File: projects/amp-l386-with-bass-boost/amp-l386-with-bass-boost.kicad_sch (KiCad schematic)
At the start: 18 parts, among them J1 AudioJack, J2 Jack-DC, U1 LM386

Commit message: Checking initial PCB placement of bassboost project
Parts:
- AudioIn1: renamed from J1; footprint jme-audio-pinheader-2.54-vertical -> jme:jme-audio-pinheader-2.54-vertical
- BassBoost1, Gain1, Volume1: footprint (none) -> Connector_PinHeader_2.54mm:PinHeader_1x03_P2.54mm_Vertical
- U1: footprint LM386:DIP08 -> Package_DIP:DIP-8_W7.62mm_Socket
- renumbered LS1 to AudioOut1, J2 to DC-9V1
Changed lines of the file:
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@@
   )
   (symbol (lib_id "Connector:AudioJack2") (at 77.47 77.47 0) (mirror x) (unit 1)
-    (in_bom yes) (on_board yes) (fields_autoplaced)
-    (property "Reference" "J1" (id 0) (at 72.39 76.8349 0)
+    (in_bom yes) (on_board yes)
+    (property "Reference" "AudioIn1" (id 0) (at 81.28 72.39 0)
       (effects (font (size 1.27 1.27)) (justify right))
     )
     (property "Value" "AudioJack" (id 1) (at 72.39 79.3749 0)
-      (effects (font (size 1.27 1.27)) (justify right))
-    )
-    (property "Footprint" "jme-audio-pinheader-2.54-vertical" (id 2) (at 77.47 77.47 0)
+      (effects (font (size 1.27 1.27)) (justify right) hide)
+    )
+    (property "Footprint" "jme:jme-audio-pinheader-2.54-vertical" (id 2) (at 77.47 77.47 0)
       (effects (font (size 1.27 1.27)) hide)
     )
@@
     (property "Reference" "U1" (id 0) (at 144.78 78.74 0))
     (property "Value" "LM386" (id 1) (at 144.78 81.28 0))
-    (property "Footprint" "LM386:DIP08" (id 2) (at 143.51 82.55 0)
+    (property "Footprint" "Package_DIP:DIP-8_W7.62mm_Socket" (id 2) (at 143.51 82.55 0)
       (effects (font (size 1.27 1.27)) hide)
     )
@@
       (effects (font (size 1.27 1.27)) (justify right))
     )
-    (property "Footprint" "" (id 2) (at 160.02 102.87 0)
+    (property "Footprint" "Connector_PinHeader_2.54mm:PinHeader_1x03_P2.54mm_Vertical" (id 2) (at 160.02 102.87 0)
       (effects (font (size 1.27 1.27)) hide)
     )
@@
   (symbol (lib_id "Device:Speaker") (at 195.58 85.09 0) (unit 1)
     (in_bom yes) (on_board yes) (fields_autoplaced)
-    (property "Reference" "LS1" (id 0) (at 200.66 85.0899 0)
+    (property "Reference" "AudioOut1" (id 0) (at 200.66 85.0899 0)
       (effects (font (size 1.27 1.27)) (justify left))
     )
@@
       (effects (font (size 1.27 1.27)) (justify right))
     )
-    (property "Footprint" "" (id 2) (at 96.52 82.55 0)
+    (property "Footprint" "Connector_PinHeader_2.54mm:PinHeader_1x03_P2.54mm_Vertical" (id 2) (at 96.52 82.55 0)
       (effects (font (size 1.27 1.27)) hide)
     )
@@
   (symbol (lib_id "Connector:Jack-DC") (at 110.49 33.02 0) (unit 1)
     (in_bom yes) (on_board yes)
-    (property "Reference" "J2" (id 0) (at 110.49 21.59 0))
-    (property "Value" "Jack-DC" (id 1) (at 110.49 24.13 0))
+    (property "Reference" "DC-9V1" (id 0) (at 110.49 26.67 0))
+    (property "Value" "Jack-DC" (id 1) (at 110.49 24.13 0)
+      (effects (font (size 1.27 1.27)) hide)
+    )
     (property "Footprint" "Connector_PinHeader_2.54mm:PinHeader_1x02_P2.54mm_Vertical" (id 2) (at 111.76 34.036 0)
       (effects (font (size 1.27 1.27)) hide)
@@
       (effects (font (size 1.27 1.27)) (justify right))
     )
-    (property "Footprint" "" (id 2) (at 157.48 119.38 0)
+    (property "Footprint" "Connector_PinHeader_2.54mm:PinHeader_1x03_P2.54mm_Vertical" (id 2) (at 157.48 119.38 0)
       (effects (font (size 1.27 1.27)) hide)
     )
@@
       (reference "#PWR0105") (unit 1) (value "GND") (footprint "")
     )
+    (path "/01ca1135-471d-4314-866e-30f63858fb82"
+      (reference "AudioIn1") (unit 1) (value "AudioJack") (footprint "jme:jme-audio-pinheader-2.54-vertical")
+    )
+    (path "/b396bfdf-cff4-4907-8efa-f00f4a874de6"
+      (reference "AudioOut1") (unit 1) (value "Speaker") (footprint "Connector_PinHeader_2.54mm:PinHeader_1x02_P2.54mm_Vertical")
+    )
     (path "/f748d3a0-8c6d-4ef5-a350-b7da4a86c917"
-      (reference "BassBoost1") (unit 1) (value "10K") (footprint "")
+      (reference "BassBoost1") (unit 1) (value "10K") (footprint "Connector_PinHeader_2.54mm:PinHeader_1x03_P2.54mm_Vertical")
     )
     (path "/56216c7c-e1fb-437a-9a94-6786f3333271"
@@
       (reference "C9") (unit 1) (value "0.033uF") (footprint "Capacitor_THT:CP_Axial_L10.0mm_D4.5mm_P15.00mm_Horizontal")
     )
+    (path "/dc59da4c-267f-4146-a600-f2cc0f4de7fd"
+      (reference "DC-9V1") (unit 1) (value "Jack-DC") (footprint "Connector_PinHeader_2.54mm:PinHeader_1x02_P2.54mm_Vertical")
+    )
     (path "/5d3052ef-966e-4509-8d8d-9f9326949027"
-      (reference "Gain1") (unit 1) (value "10K") (footprint "")
-    )
-    (path "/01ca1135-471d-4314-866e-30f63858fb82"
-      (reference "J1") (unit 1) (value "AudioJack") (footprint "jme-audio-pinheader-2.54-vertical")
-    )
-    (path "/dc59da4c-267f-4146-a600-f2cc0f4de7fd"
-      (reference "J2") (unit 1) (value "Jack-DC") (footprint "Connector_PinHeader_2.54mm:PinHeader_1x02_P2.54mm_Vertical")
-    )
-    (path "/b396bfdf-cff4-4907-8efa-f00f4a874de6"
-      (reference "LS1") (unit 1) (value "Speaker") (footprint "Connector_PinHeader_2.54mm:PinHeader_1x02_P2.54mm_Vertical")
+      (reference "Gain1") (unit 1) (value "10K") (footprint "Connector_PinHeader_2.54mm:PinHeader_1x03_P2.54mm_Vertical")
     )
     (path "/f63d6667-db21-4f94-a8c8-484525f1c0e9"
@@
     )
     (path "/23f65ee1-2ccd-4068-ae1f-1dc4d7eff59a"
-      (reference "U1") (unit 1) (value "LM386") (footprint "LM386:DIP08")
+      (reference "U1") (unit 1) (value "LM386") (footprint "Package_DIP:DIP-8_W7.62mm_Socket")
     )
     (path "/b6747b31-b318-46a5-b54d-fbc219956e2c"
-      (reference "Volume1") (unit 1) (value "10K") (footprint "")
-    )
-  )
+      (reference "Volume1") (unit 1) (value "10K") (footprint "Connector_PinHeader_2.54mm:PinHeader_1x03_P2.54mm_Vertical")
+    )
+  )

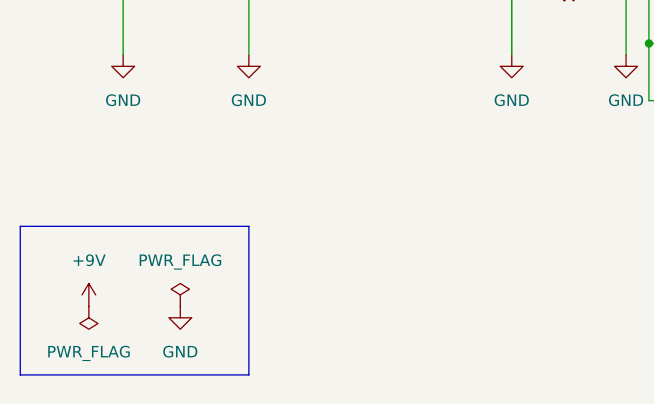
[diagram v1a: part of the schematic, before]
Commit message: Progress on amp-l386-with-bass-boost layout. Still need real footprints
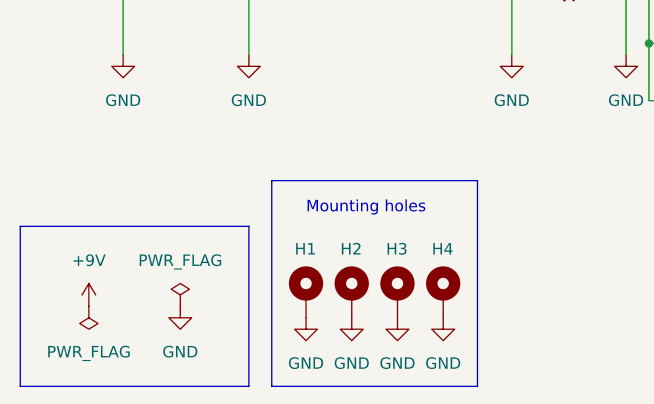
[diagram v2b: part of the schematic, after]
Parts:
- added H1, H2, H3, H4: MountingHole_Pad, MountingHole:MountingHole_3.2mm_M3_DIN965_Pad, symbol Mechanical:MountingHole_Pad
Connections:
- net GND: now also H1.1, H2.1, H3.1, H4.1
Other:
- note added: "Mounting holes"
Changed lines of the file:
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@@
+    (stroke (width 0) (type default) (color 0 0 0 0))
+  )
+  (polyline (pts (xy 121.92 147.32) (xy 99.06 147.32))
     (stroke (width 0) (type default) (color 0 0 0 0))
   )
@@
     (stroke (width 0) (type default) (color 0 0 0 0))
   )
+  (polyline (pts (xy 99.06 124.46) (xy 121.92 124.46))
+    (stroke (width 0) (type default) (color 0 0 0 0))
+  )
   (wire (pts (xy 134.62 102.87) (xy 138.43 102.87))
     (stroke (width 0) (type default) (color 0 0 0 0))
   )
-  (polyline (pts (xy 96.52 146.05) (xy 71.12 146.05))
+  (polyline (pts (xy 96.52 147.32) (xy 71.12 147.32))
     (stroke (width 0) (type default) (color 0 0 0 0))
   )
@@
     (stroke (width 0) (type default) (color 0 0 0 0))
   )
-  (polyline (pts (xy 71.12 129.54) (xy 71.12 146.05))
+  (polyline (pts (xy 71.12 129.54) (xy 71.12 147.32))
     (stroke (width 0) (type default) (color 0 0 0 0))
   )
@@
     (stroke (width 0) (type default) (color 0 0 0 0))
   )
+  (polyline (pts (xy 99.06 124.46) (xy 99.06 147.32))
+    (stroke (width 0) (type default) (color 0 0 0 0))
+  )
   (wire (pts (xy 140.97 115.57) (xy 157.48 115.57))
     (stroke (width 0) (type default) (color 0 0 0 0))
@@
     (stroke (width 0) (type default) (color 0 0 0 0))
   )
+  (polyline (pts (xy 121.92 124.46) (xy 121.92 147.32))
+    (stroke (width 0) (type default) (color 0 0 0 0))
+  )
   (wire (pts (xy 125.73 102.87) (xy 125.73 110.49))
     (stroke (width 0) (type default) (color 0 0 0 0))
@@
     (stroke (width 0) (type default) (color 0 0 0 0))
   )
-  (polyline (pts (xy 96.52 129.54) (xy 96.52 146.05))
+  (polyline (pts (xy 96.52 129.54) (xy 96.52 147.32))
     (stroke (width 0) (type default) (color 0 0 0 0))
   )
@@
   (wire (pts (xy 154.94 102.87) (xy 156.21 102.87))
     (stroke (width 0) (type default) (color 0 0 0 0))
+  )
+  (text "Mounting holes" (at 102.87 128.27 0)
+    (effects (font (size 1.27 1.27)) (justify left bottom))
   )
   (symbol (lib_id "Connector:AudioJack2") (at 77.47 77.47 0) (mirror x) (unit 1)
@@
     (pin "8")
   )
+  (symbol (lib_id "power:GND") (at 107.95 139.7 0) (unit 1)
+    (in_bom yes) (on_board yes) (fields_autoplaced)
+    (property "Reference" "#PWR08" (id 0) (at 107.95 146.05 0)
+      (effects (font (size 1.27 1.27)) hide)
+    )
+    (property "Value" "GND" (id 1) (at 107.95 144.78 0))
+    (property "Footprint" "" (id 2) (at 107.95 139.7 0)
+      (effects (font (size 1.27 1.27)) hide)
+    )
+    (property "Datasheet" "" (id 3) (at 107.95 139.7 0)
+      (effects (font (size 1.27 1.27)) hide)
+    )
+    (pin "1")
+  )
+  (symbol (lib_id "Mechanical:MountingHole_Pad") (at 102.87 137.16 0) (unit 1)
+    (in_bom yes) (on_board yes)
+    (property "Reference" "H1" (id 0) (at 101.6 132.08 0)
+      (effects (font (size 1.27 1.27)) (justify left))
+    )
+    (property "Value" "MountingHole_Pad" (id 1) (at 105.41 137.1599 0)
+      (effects (font (size 1.27 1.27)) (justify left) hide)
+    )
+    (property "Footprint" "MountingHole:MountingHole_3.2mm_M3_DIN965_Pad" (id 2) (at 102.87 137.16 0)
+      (effects (font (size 1.27 1.27)) hide)
+    )
+    (property "Datasheet" "~" (id 3) (at 102.87 137.16 0)
+      (effects (font (size 1.27 1.27)) hide)
+    )
+    (pin "1")
+  )
+  (symbol (lib_id "power:GND") (at 102.87 139.7 0) (unit 1)
+    (in_bom yes) (on_board yes) (fields_autoplaced)
+    (property "Reference" "#PWR07" (id 0) (at 102.87 146.05 0)
+      (effects (font (size 1.27 1.27)) hide)
+    )
+    (property "Value" "GND" (id 1) (at 102.87 144.78 0))
+    (property "Footprint" "" (id 2) (at 102.87 139.7 0)
+      (effects (font (size 1.27 1.27)) hide)
+    )
+    (property "Datasheet" "" (id 3) (at 102.87 139.7 0)
+      (effects (font (size 1.27 1.27)) hide)
+    )
+    (pin "1")
+  )
+  (symbol (lib_id "power:GND") (at 118.11 139.7 0) (unit 1)
+    (in_bom yes) (on_board yes) (fields_autoplaced)
+    (property "Reference" "#PWR010" (id 0) (at 118.11 146.05 0)
+      (effects (font (size 1.27 1.27)) hide)
+    )
+    (property "Value" "GND" (id 1) (at 118.11 144.78 0))
+    (property "Footprint" "" (id 2) (at 118.11 139.7 0)
+      (effects (font (size 1.27 1.27)) hide)
+    )
+    (property "Datasheet" "" (id 3) (at 118.11 139.7 0)
+      (effects (font (size 1.27 1.27)) hide)
+    )
+    (pin "1")
+  )
   (symbol (lib_id "power:PWR_FLAG") (at 88.9 138.43 0) (unit 1)
     (in_bom yes) (on_board yes) (fields_autoplaced)
@@
     (pin "2")
   )
+  (symbol (lib_id "power:GND") (at 113.03 139.7 0) (unit 1)
+    (in_bom yes) (on_board yes) (fields_autoplaced)
+    (property "Reference" "#PWR09" (id 0) (at 113.03 146.05 0)
+      (effects (font (size 1.27 1.27)) hide)
+    )
+    (property "Value" "GND" (id 1) (at 113.03 144.78 0))
+    (property "Footprint" "" (id 2) (at 113.03 139.7 0)
+      (effects (font (size 1.27 1.27)) hide)
+    )
+    (property "Datasheet" "" (id 3) (at 113.03 139.7 0)
+      (effects (font (size 1.27 1.27)) hide)
+    )
+    (pin "1")
+  )
+  (symbol (lib_id "Mechanical:MountingHole_Pad") (at 113.03 137.16 0) (unit 1)
+    (in_bom yes) (on_board yes)
+    (property "Reference" "H3" (id 0) (at 111.76 132.08 0)
+      (effects (font (size 1.27 1.27)) (justify left))
+    )
+    (property "Value" "MountingHole_Pad" (id 1) (at 115.57 137.1599 0)
+      (effects (font (size 1.27 1.27)) (justify left) hide)
+    )
+    (property "Footprint" "MountingHole:MountingHole_3.2mm_M3_DIN965_Pad" (id 2) (at 113.03 137.16 0)
+      (effects (font (size 1.27 1.27)) hide)
+    )
+    (property "Datasheet" "~" (id 3) (at 113.03 137.16 0)
+      (effects (font (size 1.27 1.27)) hide)
+    )
+    (pin "1")
+  )
   (symbol (lib_id "Device:R") (at 152.4 58.42 0) (unit 1)
     (in_bom yes) (on_board yes) (fields_autoplaced)
@@
     (pin "3")
   )
+  (symbol (lib_id "Mechanical:MountingHole_Pad") (at 107.95 137.16 0) (unit 1)
+    (in_bom yes) (on_board yes)
+    (property "Reference" "H2" (id 0) (at 106.68 132.08 0)
+      (effects (font (size 1.27 1.27)) (justify left))
+    )
+    (property "Value" "MountingHole_Pad" (id 1) (at 110.49 137.1599 0)
+      (effects (font (size 1.27 1.27)) (justify left) hide)
+    )
+    (property "Footprint" "MountingHole:MountingHole_3.2mm_M3_DIN965_Pad" (id 2) (at 107.95 137.16 0)
+      (effects (font (size 1.27 1.27)) hide)
+    )
+    (property "Datasheet" "~" (id 3) (at 107.95 137.16 0)
+      (effects (font (size 1.27 1.27)) hide)
+    )
+    (pin "1")
+  )
+  (symbol (lib_id "Mechanical:MountingHole_Pad") (at 118.11 137.16 0) (unit 1)
+    (in_bom yes) (on_board yes)
+    (property "Reference" "H4" (id 0) (at 116.84 132.08 0)
+      (effects (font (size 1.27 1.27)) (justify left))
+    )
+    (property "Value" "MountingHole_Pad" (id 1) (at 120.65 137.1599 0)
+      (effects (font (size 1.27 1.27)) (justify left) hide)
+    )
+    (property "Footprint" "MountingHole:MountingHole_3.2mm_M3_DIN965_Pad" (id 2) (at 118.11 137.16 0)
+      (effects (font (size 1.27 1.27)) hide)
+    )
+    (property "Datasheet" "~" (id 3) (at 118.11 137.16 0)
+      (effects (font (size 1.27 1.27)) hide)
+    )
+    (pin "1")
+  )
   (symbol (lib_id "power:GND") (at 171.45 67.31 0) (unit 1)
     (in_bom yes) (on_board yes) (fields_autoplaced)
@@
       (reference "#PWR06") (unit 1) (value "GND") (footprint "")
     )
+    (path "/2c9d4476-a593-4371-a480-c2002fb7297e"
+      (reference "#PWR07") (unit 1) (value "GND") (footprint "")
+    )
+    (path "/2862363a-0770-4592-bf40-b506f67a260b"
+      (reference "#PWR08") (unit 1) (value "GND") (footprint "")
+    )
+    (path "/7c023395-7320-4862-b907-3fe233b485df"
+      (reference "#PWR09") (unit 1) (value "GND") (footprint "")
+    )
+    (path "/373cb6e6-aca3-4a4c-ab4c-52a5c3b86e12"
+      (reference "#PWR010") (unit 1) (value "GND") (footprint "")
+    )
     (path "/db234f0e-ee6a-4ab3-834d-8006a58f325f"
       (reference "#PWR0101") (unit 1) (value "GND") (footprint "")
@@
       (reference "Gain1") (unit 1) (value "10K") (footprint "Connector_PinHeader_2.54mm:PinHeader_1x03_P2.54mm_Vertical")
     )
+    (path "/2bcd4b84-c63b-4058-b47f-8f47ac0dd58f"
+      (reference "H1") (unit 1) (value "MountingHole_Pad") (footprint "MountingHole:MountingHole_3.2mm_M3_DIN965_Pad")
+    )
+    (path "/b9d11159-524f-4f0c-b68b-43dbf127f834"
+      (reference "H2") (unit 1) (value "MountingHole_Pad") (footprint "MountingHole:MountingHole_3.2mm_M3_DIN965_Pad")
+    )
+    (path "/7dd87f23-341b-4f8f-b7d0-e20f292eccf5"
+      (reference "H3") (unit 1) (value "MountingHole_Pad") (footprint "MountingHole:MountingHole_3.2mm_M3_DIN965_Pad")
+    )
+    (path "/bd988001-921b-41a1-a411-bf4060cf6e03"
+      (reference "H4") (unit 1) (value "MountingHole_Pad") (footprint "MountingHole:MountingHole_3.2mm_M3_DIN965_Pad")
+    )
     (path "/f63d6667-db21-4f94-a8c8-484525f1c0e9"

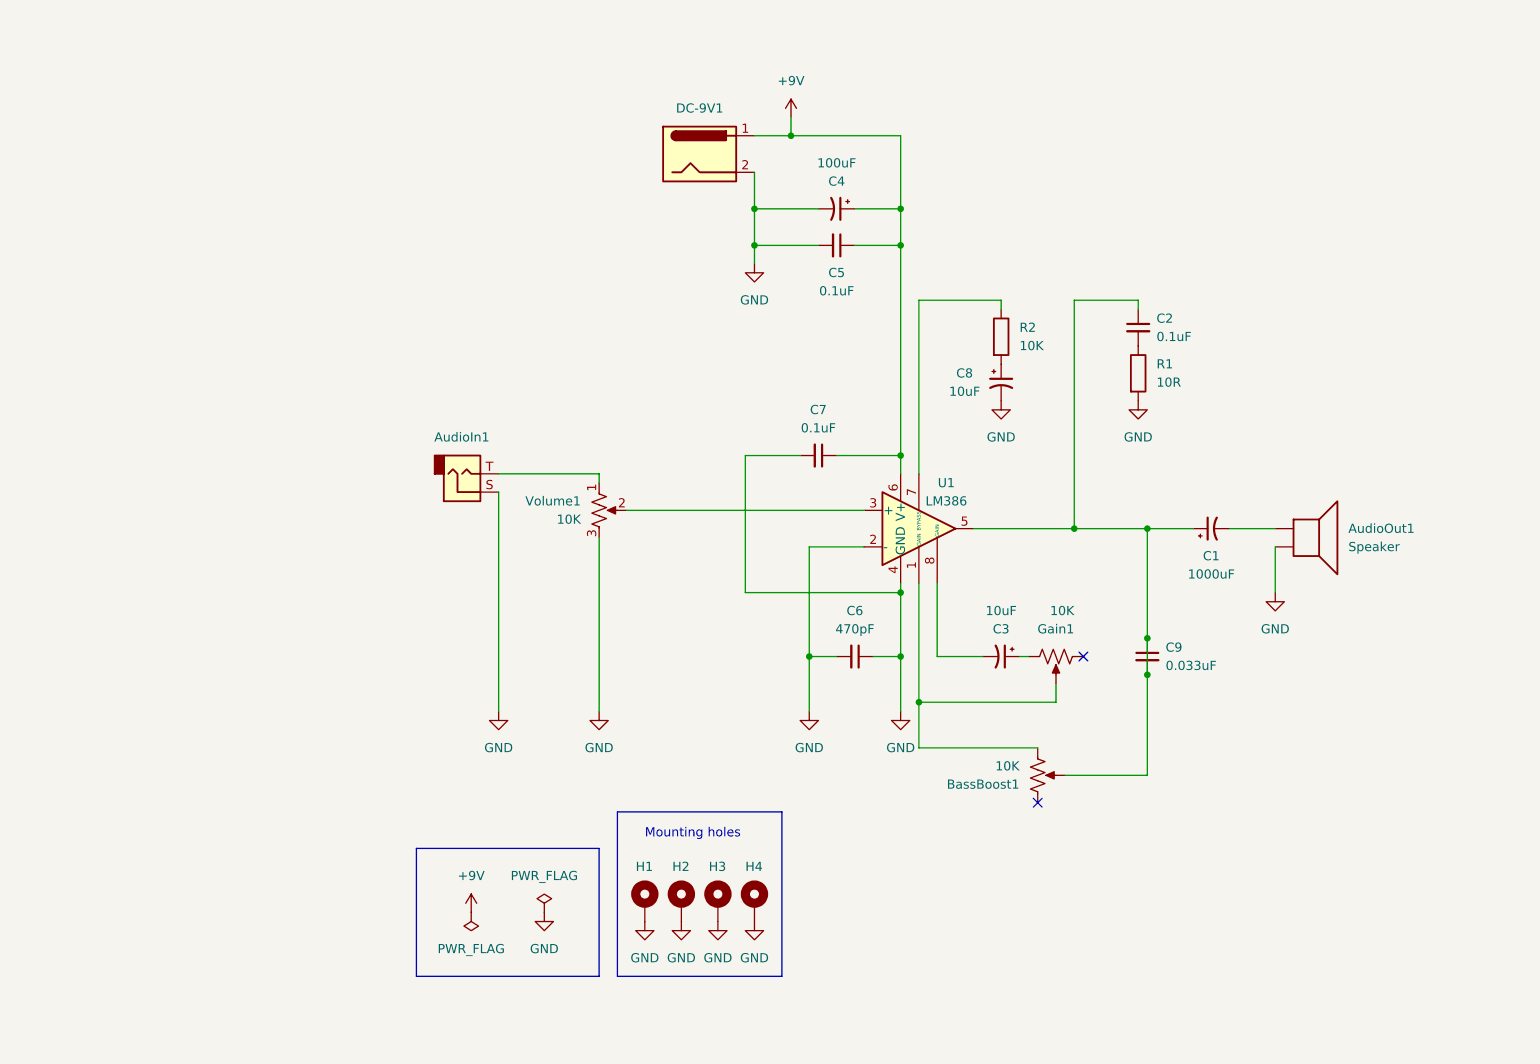
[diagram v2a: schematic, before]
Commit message: Add copper ground plane to PCB
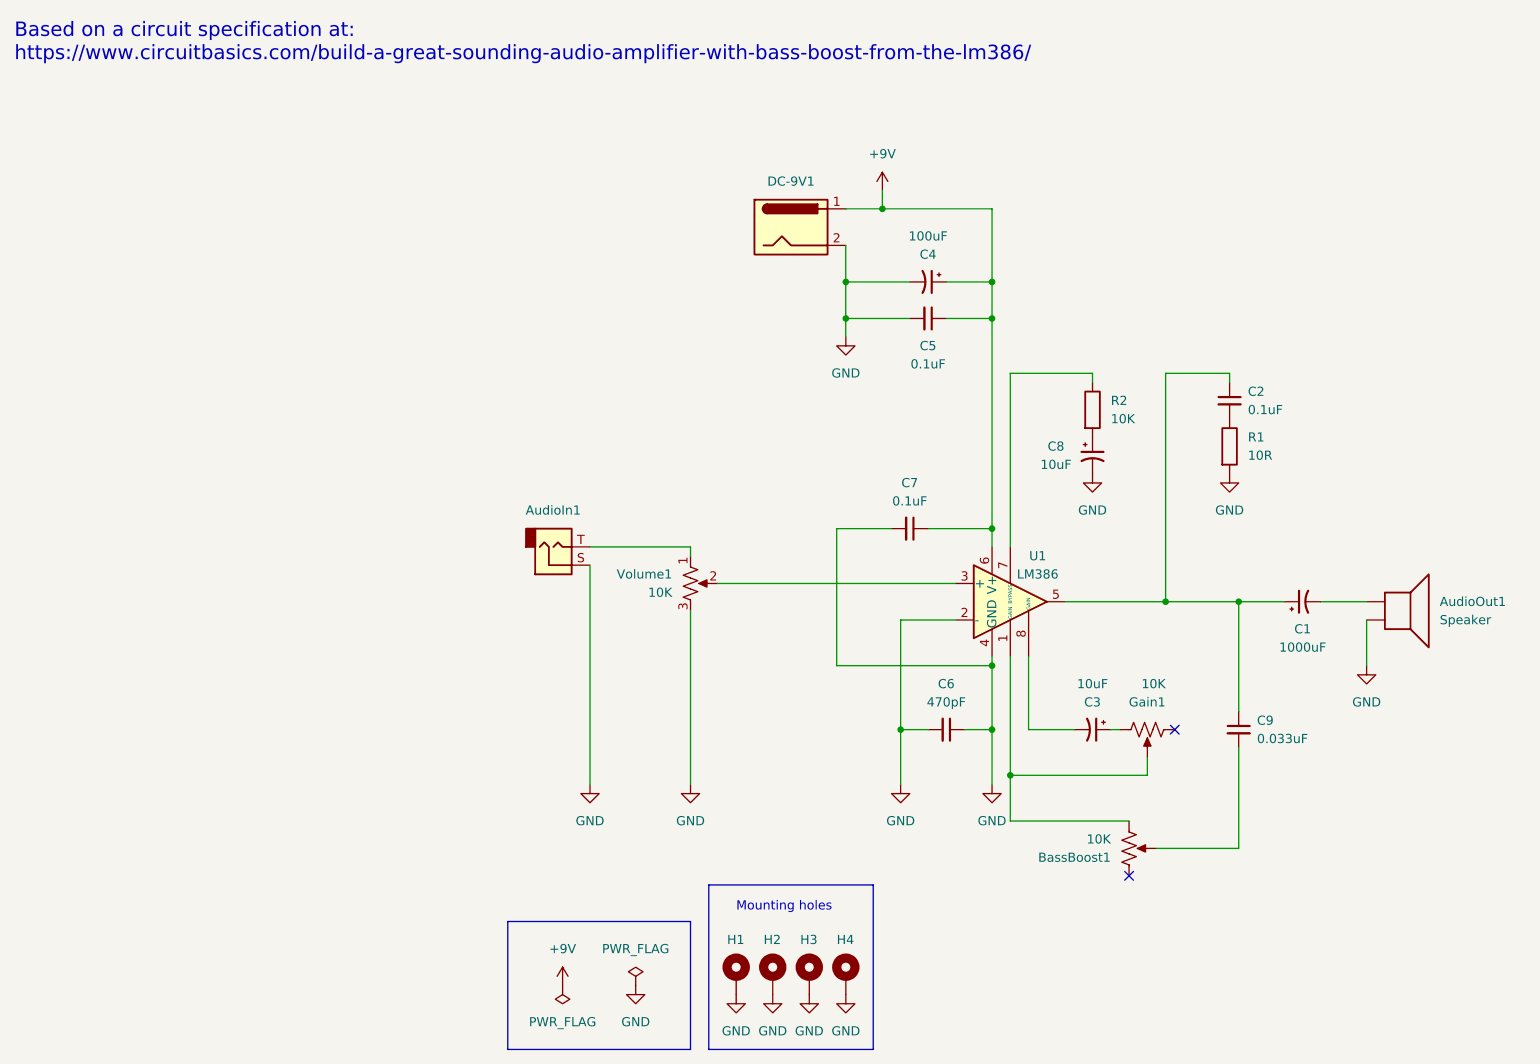
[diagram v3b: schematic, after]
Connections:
- net at C1.1, C2.1, C9.1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: no longer BassBoost1.2, C9.2
- new net: BassBoost1.2, C9.2
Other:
- note added: "Based on a circuit specification at: https://www.circuitbasics.com/build-a-great-sounding-audio-amplifier-with-bass-boost-from-the-lm386/"
- title: (none) -> amp-l386-with-bass-boost
- moved on the sheet: AudioIn1, AudioOut1, BassBoost1, C1, C2, C3, C4, C5, C6, C7, C8, C9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
